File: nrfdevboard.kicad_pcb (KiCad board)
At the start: 4 copper layers, 56 x 88 mm, 15 parts, among them J1 USB2.0, J3 Conn_01x17_Pin, J4 Conn_01x17_Pin, U1 MDBT50Q-P1MV2, Y1 32.768

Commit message: Teardrops and grid origins.
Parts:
- moved U1 5.39 mm to (101.7, 52.2)
- moved C1 5.39 mm to (113.9, 70.6)
- moved C2 5.39 mm to (110.0, 72.2)
- moved C3 5.39 mm to (106.0, 72.6)
- moved C4 5.39 mm to (98.8, 72.6)
- moved J1 5.39 mm to (105.5, 125.1)
- moved J3 5.39 mm to (132.0, 55.5)
- moved J4 5.39 mm to (84.2, 55.4)
- moved L1 5.39 mm to (109.8, 70.0)
- moved R1 5.39 mm to (113.2, 73.8)
- moved R2 5.39 mm to (110.0, 121.2)
- moved R3 5.39 mm to (108.0, 121.2)
- moved TP3 5.39 mm to (126.6, 75.8)
- moved Y1 5.39 mm to (102.4, 73.5)
- moved TP2 5.39 mm to (126.7, 70.7)
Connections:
- J1 pad 5: (no net) -> GND

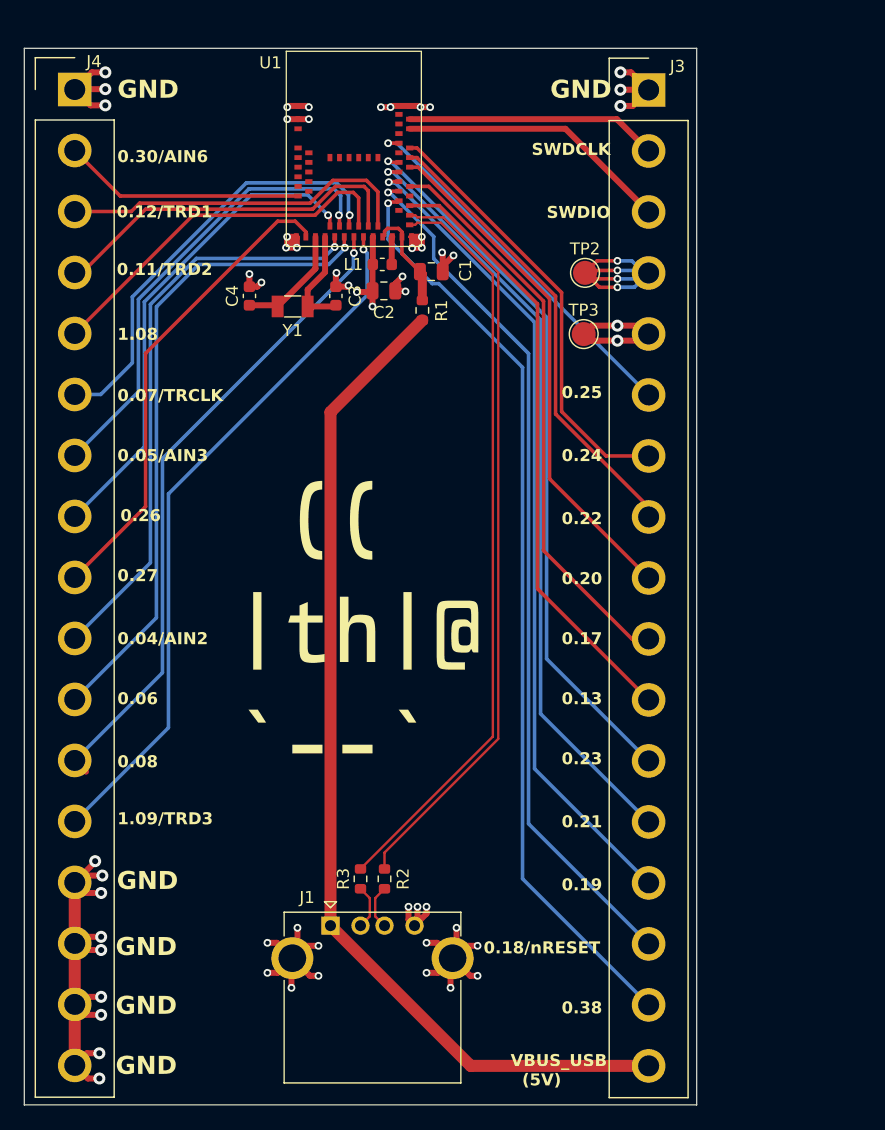
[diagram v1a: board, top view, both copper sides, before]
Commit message: PDBv2: Redesign for a framework module
V2 brings two main changes. Firstly the size has been greatly reduced to
fit into a framework module. With only 7 pins now.

Additionally, v1 had issues when running from 5v USB. I am still not
sure what this issue is since its identical to the datasheet, but I'm
now including an external voltage regulator to run the chip at 3v3. This
also reduces the BOM.
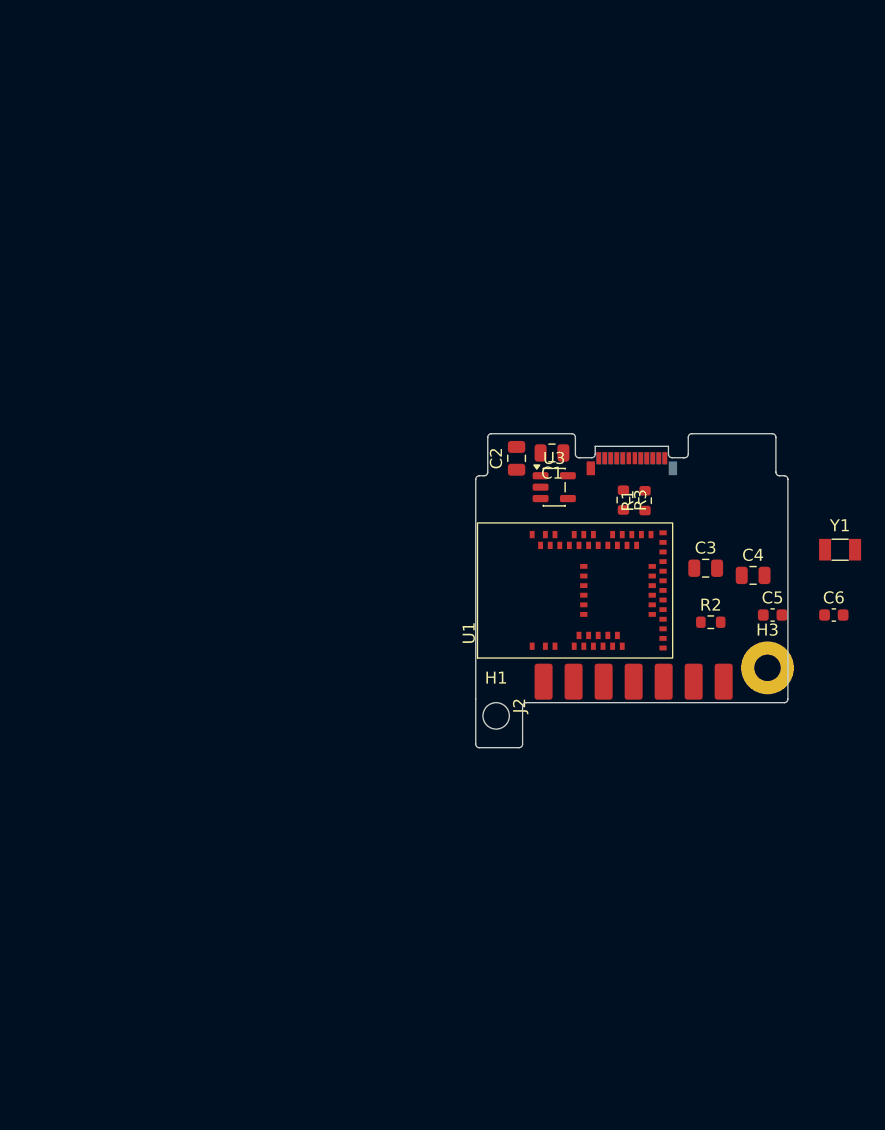
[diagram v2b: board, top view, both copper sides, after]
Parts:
- removed J1: USB2.0, Connector_USB:USB_A_Kycon_KUSBX-AS1N-B_Horizontal
- removed J3, J4: Conn_01x17_Pin, Connector_Samtec_HPM_THT:Samtec_HPM-17-01-x-S_Straight_1x17_Pitch5.08mm
- removed L1: 10uH, Inductor_SMD:L_0603_1608Metric
- removed TP2, TP3: TestPoint, TestPoint:TestPoint_Pad_D2.0mm
- added C5: 12pF, Capacitor_SMD:C_0603_1608Metric, F.Cu at (142.3, 99.2)
- added C6: 12pF, Capacitor_SMD:C_0603_1608Metric, F.Cu at (147.4, 99.2)
- added H1: MountingHole, MountingHole:MountingHole_2.2mm_M2, F.Cu at (119.3, 107.6)
- added H3: MountingHole_Pad, MountingHole:MountingHole_2.2mm_M2_Pad, F.Cu at (141.9, 103.6)
- added J2: Conn_01x07_Pin, TH-1-CC:7_side_pin, F.Cu at (121.8, 106.8)
- added REF**: USB_C_Plug_Molex_105444, Connector_USB:USB_C_Plug_Molex_105444, F.Cu at (130.6, 86.1)
- added U3: AP2112K-3.3TRG1, Package_TO_SOT_SMD:SOT-23-5, F.Cu at (124.1, 88.5)
- C3, C4: value 12pF -> 10uf; footprint Capacitor_SMD:C_0603_1608Metric -> Capacitor_SMD:C_0805_2012Metric
- R1: value 2R2 -> 5.1k
- U1: footprint TH1:TH_MDBT50Q-P1MV2 -> TH-1-CC:TH_MDBT50Q-P1MV2
- Y1: value 32.768 -> O_32.768kHz
- moved U1 53.2 mm to (117.7, 102.9), turned to 90 degrees
- moved Y1 49.9 mm to (147.9, 93.8), turned to 0 degrees
- moved C4 48.0 mm to (140.7, 95.9), turned to 0 degrees
- moved R3 38.4 mm to (129.9, 89.6), turned to -90 degrees
- moved C3 38.2 mm to (136.8, 95.3), turned to 0 degrees
- moved R2 34.6 mm to (137.2, 99.8), turned to 0 degrees
- moved R1 24.4 mm to (131.7, 89.7)
- moved C1 18.1 mm to (124.0, 85.7), turned to 180 degrees
- moved C2 17.8 mm to (121.0, 86.2), turned to 90 degrees
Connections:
- C1 pad 1: /VBUS -> +3.3V
- C2 pad 1: /3v3 -> VBUS
- C3 pad 2: /XL2 -> Net-(U1B-VDD)
- C4 pad 1: /XL1 -> Net-(U1B-VBUS)
- R1 pad 1: /VBUS_USB -> Net-(P1-CC)
- R1 pad 2: /VBUS -> GND
- R2 pad 1: /c_D+ -> D-
- R2 pad 2: /D+ -> Net-(U1A-D-)
- R3 pad 1: /c_D- -> D+
- R3 pad 2: /D- -> Net-(U1A-D+)
- U1 pad 14: /0.30/AIN6 -> unconnected-(U1A-P0.30/AIN6-Pad14)
- U1 pad 16: /0.27 -> unconnected-(U1A-P0.27-Pad16)
- U1 pad 17: /XL1 -> Net-(U1A-P0.0/XL1)
- U1 pad 18: /XL2 -> Net-(U1A-P0.01/XL2)
- U1 pad 19: /0.26 -> unconnected-(U1A-P0.26-Pad19)
- U1 pad 20: /0.04/AIN2 -> unconnected-(U1A-P0.04/AIN2-Pad20)
- U1 pad 21: /0.05/AIN3 -> unconnected-(U1A-P0.05/AIN3-Pad21)
- U1 pad 22: /0.06 -> unconnected-(U1A-P0.06-Pad22)
- U1 pad 23: /0.07/TRCLK -> unconnected-(U1A-P0.07/TRACECLK-Pad23)
- U1 pad 24: /0.08 -> unconnected-(U1A-P0.08-Pad24)
- U1 pad 25: /1.08 -> unconnected-(U1A-P1.08-Pad25)
- U1 pad 26: /1.09/TRD3 -> unconnected-(U1A-P1.09/TRACEDATA3-Pad26)
- U1 pad 27: /0.11/TRD2 -> unconnected-(U1A-P0.11/TRACEDATA2-Pad27)
- U1 pad 28: /3v3 -> Net-(U1B-VDD)
- U1 pad 29: /0.12/TRD1 -> unconnected-(U1A-P0.12/TRACEDATA1-Pad29)
- U1 pad 30: /VBUS -> Net-(U1B-VDD)
- U1 pad 31: /DCCH -> unconnected-(U1B-DCCH-Pad31)
- U1 pad 32: /VBUS -> Net-(U1B-VBUS)
- U1 pad 34: /D- -> Net-(U1A-D-)
- U1 pad 35: /D+ -> Net-(U1A-D+)
- U1 pad 37: /0.13 -> unconnected-(U1A-P0.13-Pad37)
- U1 pad 38: /0.38 -> unconnected-(U1A-P0.16-Pad38)
- U1 pad 40: /0.18/nRESET -> unconnected-(U1A-P0.18/nRESET-Pad40)
- U1 pad 41: /0.17 -> unconnected-(U1A-P0.17-Pad41)
- U1 pad 42: /0.19 -> unconnected-(U1A-P0.19-Pad42)
- U1 pad 43: /0.21 -> unconnected-(U1A-P0.21-Pad43)
- U1 pad 44: /0.20 -> unconnected-(U1A-P0.20-Pad44)
- U1 pad 45: /0.23 -> unconnected-(U1A-PO23-Pad45)
- U1 pad 46: /0.22 -> unconnected-(U1A-P0.22-Pad46)
- U1 pad 48: /0.24 -> unconnected-(U1A-P0.24-Pad48)
- U1 pad 49: /0.25 -> unconnected-(U1A-P0.25-Pad49)
- U1 pad 51: /SWDIO -> unconnected-(U1A-SWDIO-Pad51)
- U1 pad 53: /SWDCLK -> unconnected-(U1A-SWDCLK-Pad53)
- Y1 pad 1: /XL1 -> Net-(U1A-P0.01/XL2)
- Y1 pad 2: /XL2 -> Net-(U1A-P0.0/XL1)
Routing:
- net GND: track 135.8 -> 0.00 mm, vias 54 -> 0
- net /VBUS_USB: track 84.9 -> 0.00 mm
- net /0.38: track 77.1 -> 0.00 mm, vias 1 -> 0
- net /0.18/nRESET: track 72.6 -> 0.00 mm, vias 1 -> 0
- net /0.19: track 68.6 -> 0.00 mm, vias 1 -> 0
- net /0.21: track 64.2 -> 0.00 mm, vias 1 -> 0
- net /D+: track 63.0 -> 0.00 mm
- net /D-: track 62.9 -> 0.00 mm
- net /0.23: track 60.0 -> 0.00 mm, vias 1 -> 0
- net /1.09/TRD3: track 59.0 -> 0.00 mm, vias 1 -> 0
- net /0.08: track 55.7 -> 0.00 mm, vias 1 -> 0
- net /0.06: track 54.2 -> 0.00 mm, vias 1 -> 0
- net /0.13: track 50.9 -> 0.00 mm
- net /0.04/AIN2: track 48.6 -> 0.00 mm, vias 1 -> 0
- net /0.17: track 47.7 -> 0.00 mm
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- added copper zone on In2.Cu, net (none)
- removed copper zone on In2.Cu, net /3v3
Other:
- board size 56 x 88 mm -> 26 x 26.2 mm
- board text removed: "0.04/AIN2"
- board text removed: "0.05/AIN3"
- board text removed: "0.06"
- board text removed: "0.07/TRCLK"
- board text removed: "0.08"
- board text removed: "0.11/TRD2"
- board text removed: "0.12/TRD1"
- board text removed: "0.13"
- board text removed: "0.17"
- board text removed: "0.18/nRESET"
- board text removed: "0.19"
- board text removed: "0.20"
- board text removed: "0.21"
- board text removed: "0.22"
- board text removed: "0.23"
- board text removed: "0.24"
- board text removed: "0.25"
- board text removed: "0.26"
- board text removed: "0.27"
- board text removed: "0.30/AIN6"
- board text removed: "0.38"
- board text removed: "1.08"
- board text removed: "1.09/TRD3"
- board text removed: "GND"
- board text removed: "SWDCLK"
- board text removed: "SWDIO"
- board text removed: "VBUS_USB (5V)"

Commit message: Minor tweaks
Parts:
- added TP1: TestPoint, TestPoint:TestPoint_Pad_D1.0mm, B.Cu at (113.2, 95.8)
- moved Y1 12.7 mm to (136.2, 98.5), turned to 90 degrees
- moved R2 11.0 mm to (132.8, 89.8), turned to 90 degrees
- moved C6 10.7 mm to (137.0, 101.5)
- moved C5 6.30 mm to (137.2, 95.6), turned to 180 degrees
- moved C4 5.84 mm to (136.8, 91.6)
- moved C1 4.80 mm to (124.0, 90.5)
- moved R1 3.80 mm to (128.0, 88.9), turned to 180 degrees
- moved C3 1.70 mm to (136.8, 93.6)
- moved R3 1.11 mm to (131.0, 89.8)
- moved U3 0.80 mm to (124.1, 87.8), turned to 180 degrees
- moved C2 0.10 mm to (121.0, 86.2), turned to -90 degrees
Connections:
- net Net-(U1A-D+) renamed /D+_r
- net Net-(U1A-D-) renamed /D-_r
- net Net-(U1A-P0.01/XL2) renamed /XL2
- net Net-(U1A-P0.0/XL1) renamed /XL1
- C3 pad 1: GND -> +3.3V
- C3 pad 2: Net-(U1B-VDD) -> GND
- C4 pad 1: Net-(U1B-VBUS) -> VBUS
- U1 pad 28: Net-(U1B-VDD) -> +3.3V
- U1 pad 30: Net-(U1B-VDD) -> +3.3V
- U1 pad 32: Net-(U1B-VBUS) -> VBUS
- U1 pad 40: unconnected-(U1A-P0.18/nRESET-Pad40) -> Net-(U1A-P0.18/nRESET)

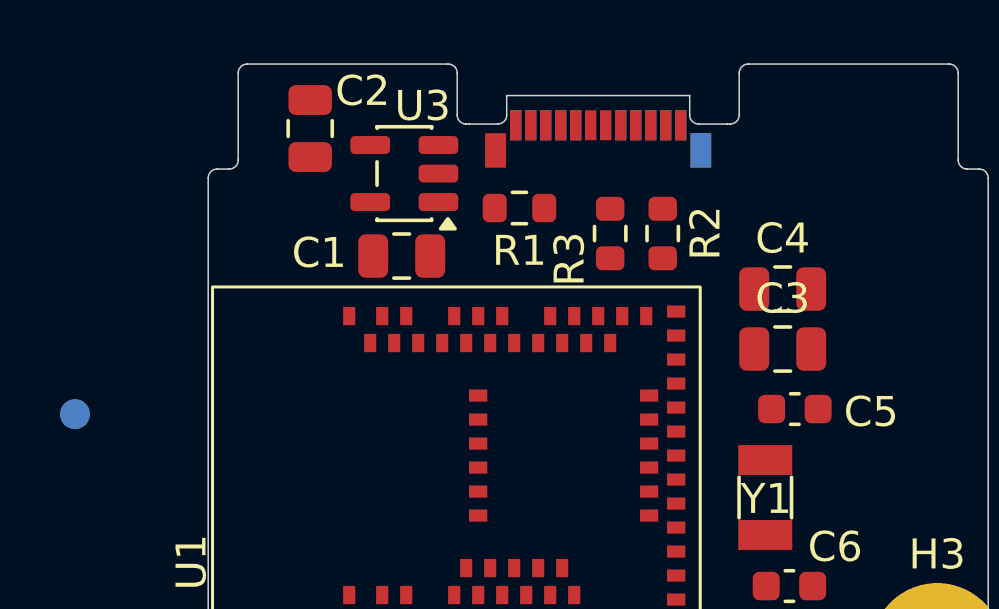
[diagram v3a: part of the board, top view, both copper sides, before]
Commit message: Add fw expansion case and proper usbc footprint
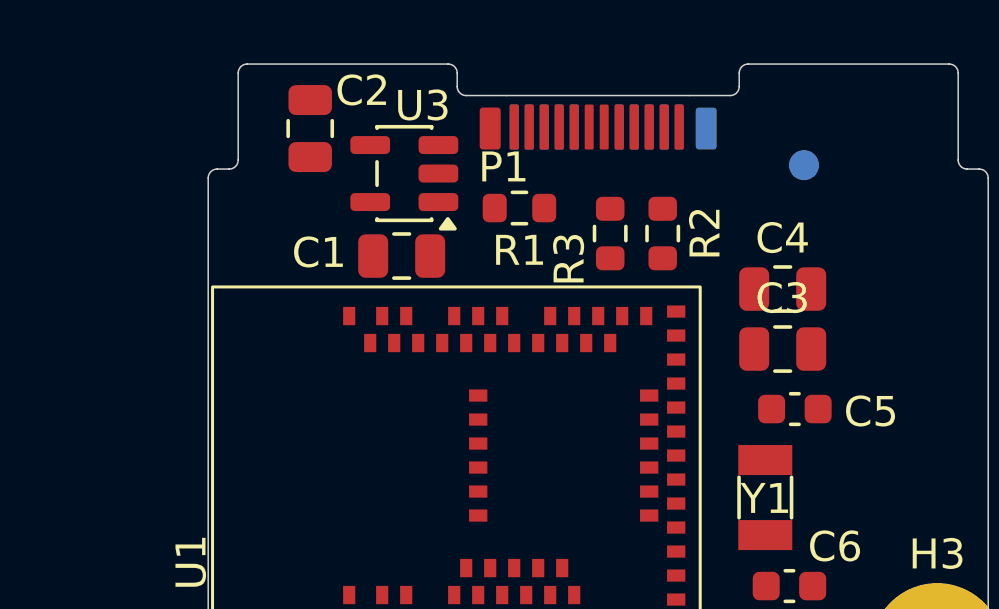
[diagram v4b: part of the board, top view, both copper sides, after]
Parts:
- removed REF**: USB_C_Plug_Molex_105444, Connector_USB:USB_C_Plug_Molex_105444
- added P1: USB_C_Plug_USB2.0, TH-1-CC:USBC, F.Cu at (126.5, 85.5)
- moved TP1 25.7 mm to (137.5, 87.5)
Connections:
- J2 pad 1: PIN2 -> PIN1
- J2 pad 2: PIN3 -> PIN2
- J2 pad 3: PIN4 -> PIN3
- J2 pad 4: PIN5 -> PIN4
- J2 pad 5: PIN6 -> PIN5
- J2 pad 6: PIN7 -> PIN6
- R1 pad 1: Net-(P1-CC) -> /CC
- U1 pad 51: unconnected-(U1A-SWDIO-Pad51) -> PIN2
- U1 pad 53: unconnected-(U1A-SWDCLK-Pad53) -> PIN1
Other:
- outline, holes or cut-outs redrawn

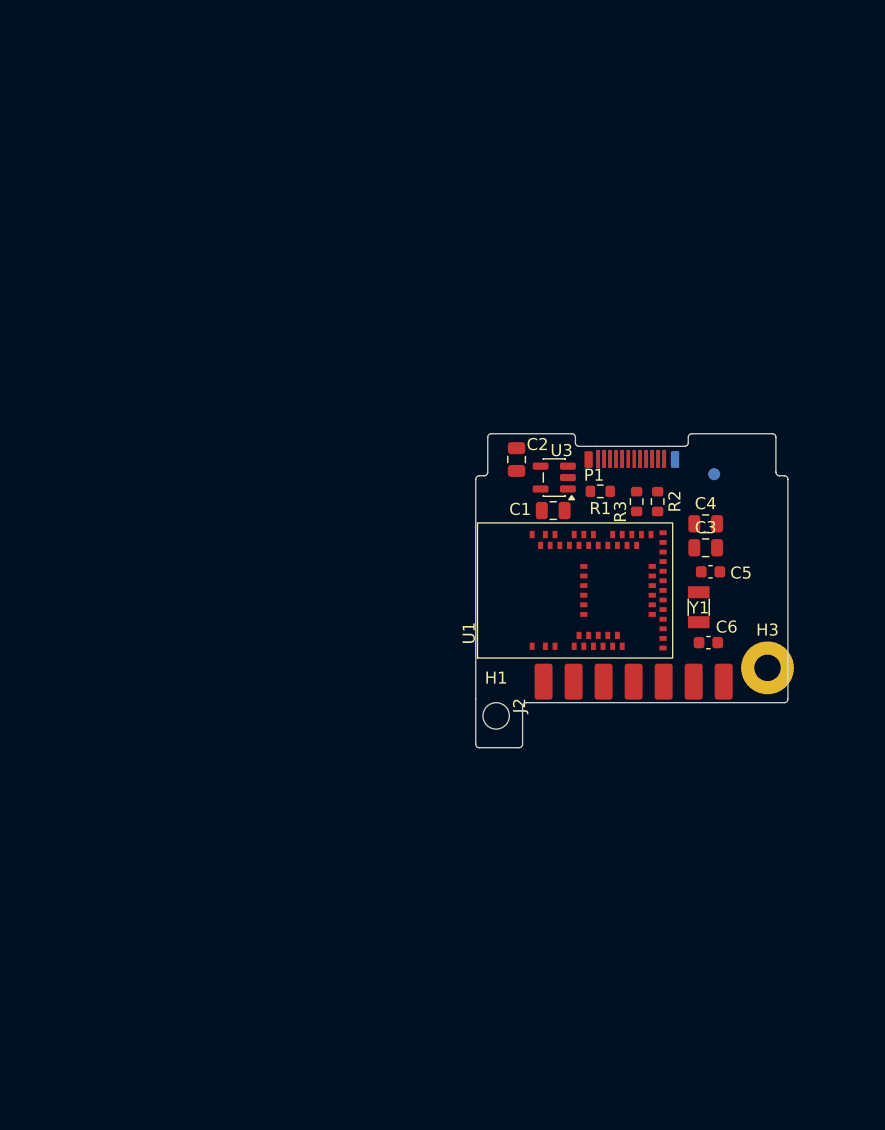
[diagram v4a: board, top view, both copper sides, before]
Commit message: Initial routing + 7 more GPIO pins
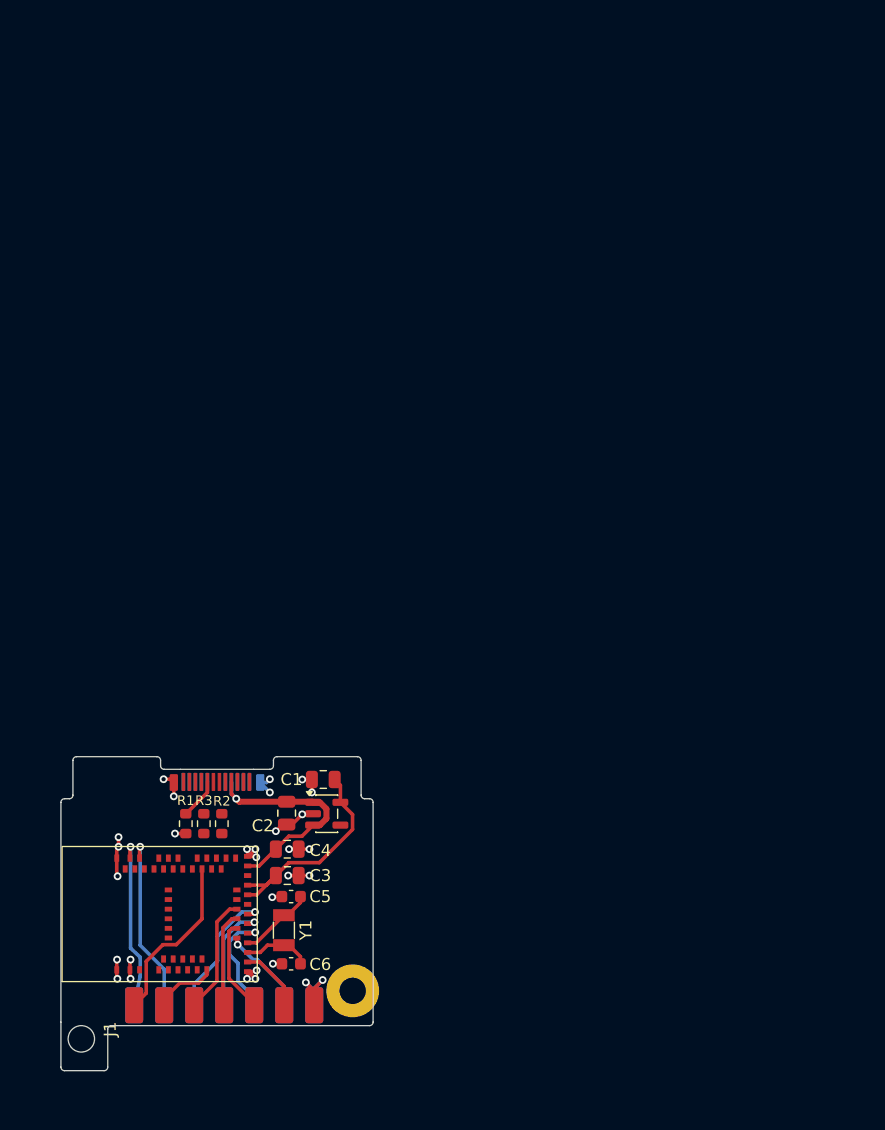
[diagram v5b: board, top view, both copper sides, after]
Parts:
- removed TP1: TestPoint, TestPoint:TestPoint_Pad_D1.0mm
- added J1: Conn_01x07_Pin, TH-1-CC:7_side_pin, F.Cu at (87.7, 133.7)
- J2: moved to B.Cu
- moved R2 45.1 mm to (96.5, 116.6), turned to -90 degrees
- moved R3 44.9 mm to (95.0, 116.6)
- moved C3 44.3 mm to (101.9, 120.9)
- moved R1 44.2 mm to (93.5, 116.6), turned to -90 degrees
- moved C5 44.2 mm to (102.2, 122.7), turned to 0 degrees
- moved C4 44.1 mm to (101.9, 118.7)
- moved U1 43.9 mm to (83.1, 129.9)
- moved C6 43.9 mm to (102.2, 128.2), turned to 180 degrees
- moved H3 43.8 mm to (107.3, 130.5)
- moved H1 43.8 mm to (84.8, 134.5)
- moved P1 43.8 mm to (92.0, 112.3)
- moved Y1 43.8 mm to (101.6, 125.5)
- moved J2 41.1 mm to (87.7, 129.7), turned to -90 degrees
- moved C2 35.1 mm to (101.8, 115.7)
- moved U3 33.8 mm to (105.2, 115.8), turned to 0 degrees
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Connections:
- U1 pad 14: unconnected-(U1A-P0.30/AIN6-Pad14) -> PIN9
- U1 pad 16: unconnected-(U1A-P0.27-Pad16) -> PIN13
- U1 pad 19: unconnected-(U1A-P0.26-Pad19) -> PIN6
- U1 pad 20: unconnected-(U1A-P0.04/AIN2-Pad20) -> PIN5
- U1 pad 21: unconnected-(U1A-P0.05/AIN3-Pad21) -> PIN12
- U1 pad 22: unconnected-(U1A-P0.06-Pad22) -> PIN4
- U1 pad 23: unconnected-(U1A-P0.07/TRACECLK-Pad23) -> PIN11
- U1 pad 24: unconnected-(U1A-P0.08-Pad24) -> PIN3
- U1 pad 25: unconnected-(U1A-P1.08-Pad25) -> PIN10
- U1 pad 40: Net-(U1A-P0.18/nRESET) -> PIN8
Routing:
- net GND: track 0.00 -> 36.1 mm, vias 0 -> 30
- net VBUS: track 0.00 -> 20.0 mm, vias 0 -> 1
- net +3.3V: track 0.00 -> 18.5 mm
- net PIN2: track 0.00 -> 15.0 mm, vias 0 -> 1
- net PIN1: track 0.00 -> 15.0 mm, vias 0 -> 1
- net PIN8: track 0.00 -> 14.3 mm
- net PIN3: track 0.00 -> 11.2 mm, vias 0 -> 1
- net PIN10: track 0.00 -> 9.82 mm
- net PIN4: track 0.00 -> 9.32 mm, vias 0 -> 1
- net PIN5: track 0.00 -> 9.29 mm, vias 0 -> 1
- net PIN11: track 0.00 -> 7.96 mm
- net PIN12: track 0.00 -> 7.78 mm
- net PIN6: track 0.00 -> 7.46 mm, vias 0 -> 1
- net /XL2: track 0.00 -> 6.29 mm
- net /XL1: track 0.00 -> 5.64 mm
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- removed copper zone on In2.Cu, net (none)
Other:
- outline, holes or cut-outs redrawn
